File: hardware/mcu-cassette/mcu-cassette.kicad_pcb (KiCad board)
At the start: 2 copper layers, 80.4 x 50 mm, 11 parts, among them U1 02x15_PIN_HEADER_SOCKET

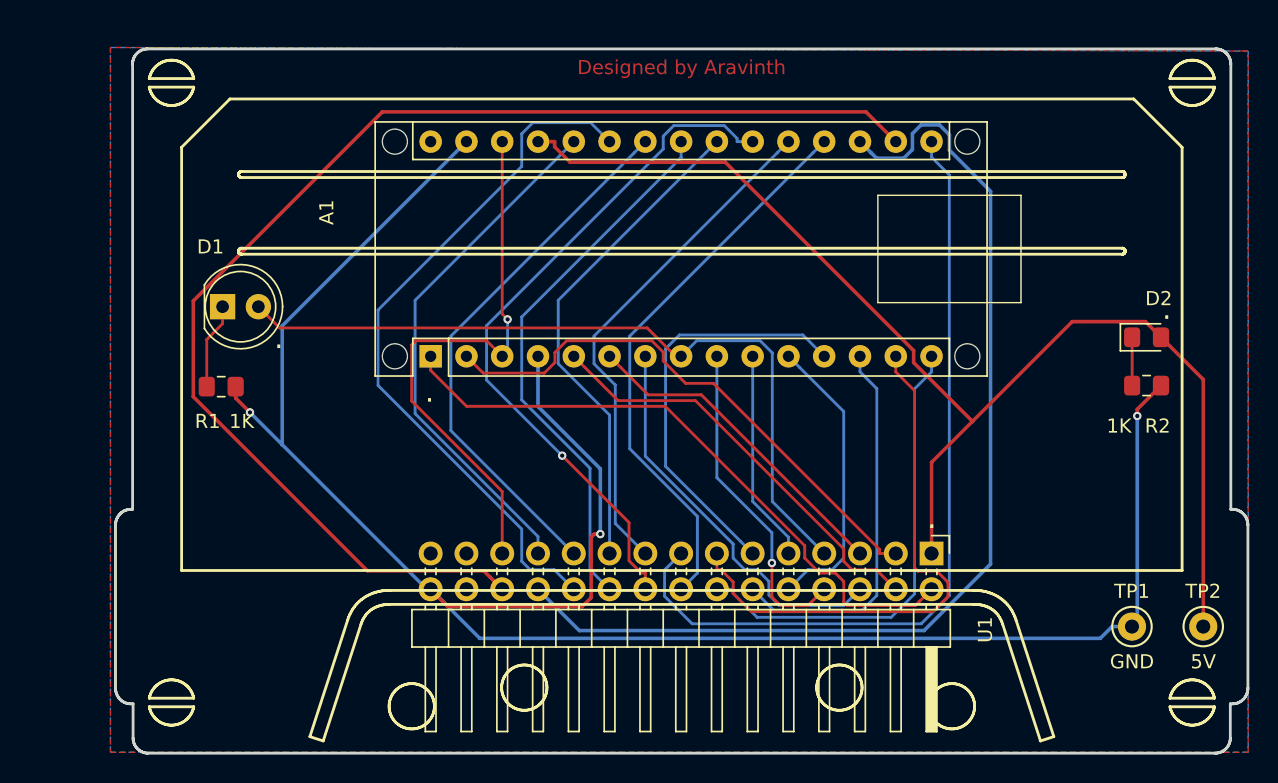
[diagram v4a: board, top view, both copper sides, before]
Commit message: [hw] Make MCU Module production ready
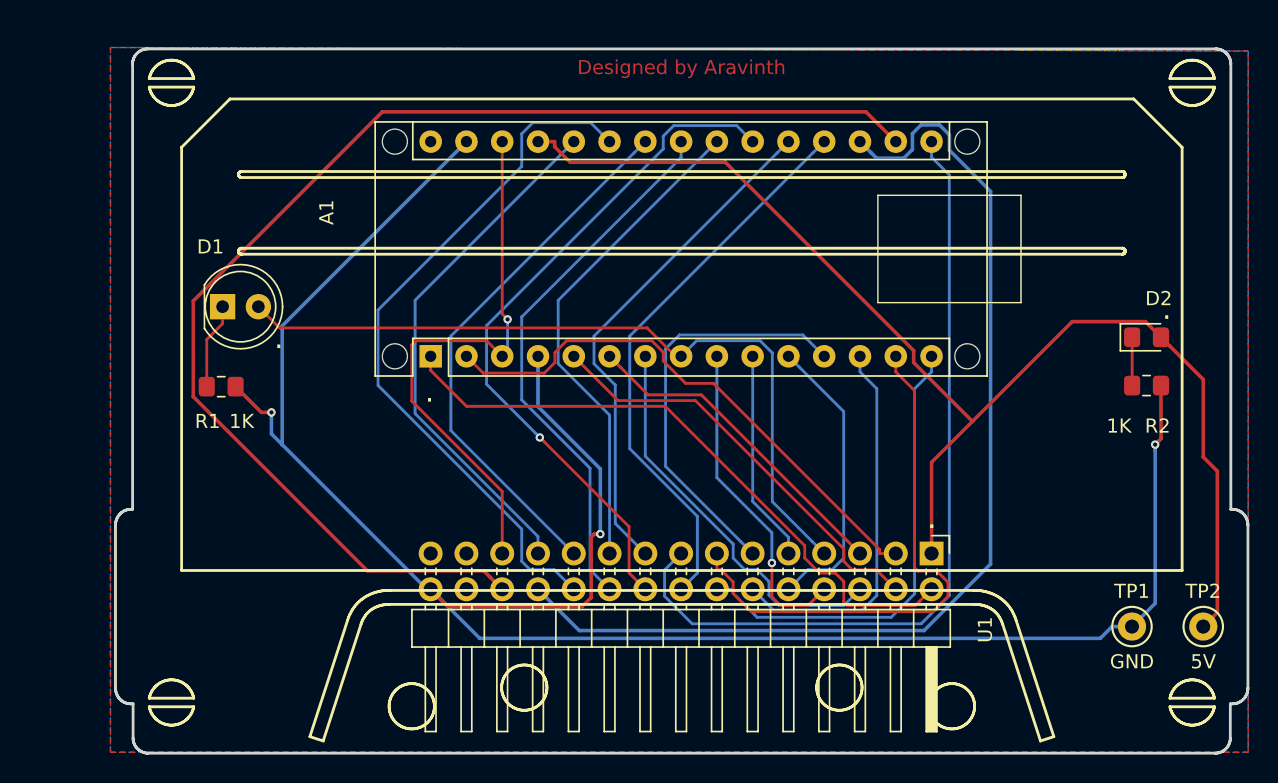
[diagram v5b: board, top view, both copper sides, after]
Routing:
- net 5V: track 88.9 -> 89.8 mm
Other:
- board text added: "MCU Module v0.1 : Designed by Aravinth"
- board text removed: "ECG Module v0.2 : Designed by Aravinth"
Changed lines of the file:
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@@
     (thickness 1.6)
     (drawings 7)
-    (tracks 256)
+    (tracks 263)
     (zones 0)
     (modules 11)
@@
     (visible_elements FFFFFF7F)
     (pcbplotparams
-      (layerselection 0x010fc_ffffffff)
-      (usegerberextensions false)
+      (layerselection 0x010f0_ffffffff)
+      (usegerberextensions true)
       (usegerberattributes false)
       (usegerberadvancedattributes false)
       (creategerberjobfile false)
-      (excludeedgelayer true)
+      (excludeedgelayer false)
       (linewidth 0.100000)
       (plotframeref false)
@@
       (plotinvisibletext false)
       (padsonsilk false)
-      (subtractmaskfromsilk false)
+      (subtractmaskfromsilk true)
       (outputformat 1)
       (mirror false)
-      (drillshape 1)
+      (drillshape 0)
       (scaleselection 1)
-      (outputdirectory ""))
+      (outputdirectory "gerber/"))
   )
   (net 0 "")
@@
     (effects (font (size 1.5 1.5) (thickness 0.3)) (justify mirror))
   )
-  (gr_text "ECG Module v0.2 : Designed by Aravinth" (at 140.4112 111.90732) (layer B.SilkS)
+  (gr_text "MCU Module v0.1 : Designed by Aravinth" (at 140.4112 111.90732) (layer B.SilkS)
     (effects (font (size 1.5 1.5) (thickness 0.3)) (justify mirror))
   )
@@
   (segment (start 140.335 138.54) (end 141.489801 137.385199) (width 0.2032) (layer B.Cu) (net 5) (status 10))
   (segment (start 172.344 141.188) (end 171.4965 141.188) (width 0.254) (layer F.Cu) (net 6) (status 30))
-  (segment (start 108.708 124.964) (end 109.728 125.984) (width 0.254) (layer F.Cu) (net 6))
-  (via (at 109.728 125.984) (size 0.6) (drill 0.3) (layers F.Cu B.Cu) (net 6))
-  (segment (start 108.708 124.155) (end 108.708 124.964) (width 0.254) (layer F.Cu) (net 6) (status 10))
   (segment (start 122.284 138.54) (end 122.555 138.54) (width 0.254) (layer B.Cu) (net 6) (status 30))
   (segment (start 112.014 119.841) (end 112.014 128.27) (width 0.254) (layer B.Cu) (net 6))
   (segment (start 112.014 128.27) (end 122.284 138.54) (width 0.254) (layer B.Cu) (net 6) (status 20))
   (segment (start 125.095 106.76) (end 112.014 119.841) (width 0.254) (layer B.Cu) (net 6) (status 10))
-  (segment (start 109.728 125.984) (end 112.014 128.27) (width 0.254) (layer B.Cu) (net 6))
   (segment (start 170.929787 141.188) (end 172.344 141.188) (width 0.254) (layer B.Cu) (net 6) (status 20))
   (segment (start 126.03801 142.02301) (end 170.094777 142.02301) (width 0.254) (layer B.Cu) (net 6))
   (segment (start 170.094777 142.02301) (end 170.929787 141.188) (width 0.254) (layer B.Cu) (net 6))
   (segment (start 122.555 138.54) (end 126.03801 142.02301) (width 0.254) (layer B.Cu) (net 6) (status 10))
-  (via (at 172.72 126.238) (size 0.6) (drill 0.3) (layers F.Cu B.Cu) (net 6))
-  (segment (start 172.72 125.764) (end 172.72 126.238) (width 0.254) (layer F.Cu) (net 6))
-  (segment (start 174.405 124.079) (end 172.72 125.764) (width 0.254) (layer F.Cu) (net 6) (status 10))
-  (segment (start 172.72 140.812) (end 172.344 141.188) (width 0.254) (layer B.Cu) (net 6) (status 30))
-  (segment (start 172.72 126.238) (end 172.72 140.812) (width 0.254) (layer B.Cu) (net 6) (status 20))
   (segment (start 134.5994 129.990288) (end 134.5994 134.62) (width 0.254) (layer B.Cu) (net 6))
   (via (at 134.5994 134.62) (size 0.6) (drill 0.3) (layers F.Cu B.Cu) (net 6))
@@
   (segment (start 133.946001 136.398) (end 133.946001 136.590881) (width 0.254) (layer F.Cu) (net 6))
   (segment (start 133.946001 134.849135) (end 133.946001 136.398) (width 0.254) (layer F.Cu) (net 6))
+  (via (at 173.99 128.27) (size 0.6) (drill 0.3) (layers F.Cu B.Cu) (net 6))
+  (segment (start 174.289999 127.970001) (end 173.99 128.27) (width 0.254) (layer F.Cu) (net 6))
+  (segment (start 174.405 124.079) (end 174.405 127.855) (width 0.254) (layer F.Cu) (net 6))
+  (segment (start 172.344 141.188) (end 173.99 139.542) (width 0.254) (layer B.Cu) (net 6))
+  (segment (start 174.405 127.855) (end 174.289999 127.970001) (width 0.254) (layer F.Cu) (net 6))
+  (segment (start 173.99 139.542) (end 173.99 128.694264) (width 0.254) (layer B.Cu) (net 6))
+  (segment (start 173.99 128.694264) (end 173.99 128.27) (width 0.254) (layer B.Cu) (net 6))
+  (via (at 111.252012 125.984) (size 0.6) (drill 0.3) (layers F.Cu B.Cu) (net 6))
+  (segment (start 111.252012 127.508012) (end 111.252012 126.408264) (width 0.254) (layer B.Cu) (net 6))
+  (segment (start 111.252012 126.408264) (end 111.252012 125.984) (width 0.254) (layer B.Cu) (net 6))
+  (segment (start 110.537 125.984) (end 110.827748 125.984) (width 0.254) (layer F.Cu) (net 6))
+  (segment (start 108.708 124.155) (end 110.537 125.984) (width 0.254) (layer F.Cu) (net 6))
+  (segment (start 110.827748 125.984) (end 111.252012 125.984) (width 0.254) (layer F.Cu) (net 6))
+  (segment (start 112.014 128.27) (end 111.252012 127.508012) (width 0.254) (layer B.Cu) (net 6))
   (segment (start 147.155001 107.559999) (end 147.955 106.76) (width 0.2032) (layer B.Cu) (net 7) (status 30))
   (segment (start 134.150199 122.530305) (end 134.150199 120.564801) (width 0.2032) (layer B.Cu) (net 7))
@@
   (segment (start 151.880199 136.554305) (end 151.880199 135.676093) (width 0.2032) (layer F.Cu) (net 8))
   (segment (start 155.575 138.54) (end 154.189801 137.154801) (width 0.2032) (layer F.Cu) (net 8) (status 10))
-  (segment (start 137.795 137.3849) (end 137.5061 137.3849) (width 0.2032) (layer F.Cu) (net 9))
-  (segment (start 136.6399 136.5187) (end 136.6399 133.801) (width 0.2032) (layer F.Cu) (net 9))
-  (segment (start 137.795 138.54) (end 137.795 137.3849) (width 0.2032) (layer F.Cu) (net 9) (status 10))
-  (segment (start 137.5061 137.3849) (end 136.6399 136.5187) (width 0.2032) (layer F.Cu) (net 9))
-  (segment (start 136.6399 133.801) (end 131.8919 129.053) (width 0.2032) (layer F.Cu) (net 9))
-  (via (at 131.8919 129.053) (size 0.6) (drill 0.3) (layers F.Cu B.Cu) (net 9))
-  (segment (start 144.3099 106.76) (end 144.3099 106.531) (width 0.2032) (layer B.Cu) (net 9))
-  (segment (start 139.065 106.3716) (end 139.065 107.2798) (width 0.2032) (layer B.Cu) (net 9))
-  (segment (start 126.5255 119.8193) (end 126.5255 123.6866) (width 0.2032) (layer B.Cu) (net 9))
-  (segment (start 144.3099 106.531) (end 143.4005 105.6216) (width 0.2032) (layer B.Cu) (net 9))
-  (segment (start 139.815 105.6216) (end 139.065 106.3716) (width 0.2032) (layer B.Cu) (net 9))
-  (segment (start 143.4005 105.6216) (end 139.815 105.6216) (width 0.2032) (layer B.Cu) (net 9))
-  (segment (start 145.415 106.76) (end 144.3099 106.76) (width 0.2032) (layer B.Cu) (net 9) (status 10))
+  (via (at 130.302 127.762) (size 0.6) (drill 0.3) (layers F.Cu B.Cu) (net 9))
+  (segment (start 137.795 138.54) (end 136.6399 137.3849) (width 0.2032) (layer F.Cu) (net 9))
+  (segment (start 136.6399 134.0999) (end 130.601999 128.061999) (width 0.2032) (layer F.Cu) (net 9))
+  (segment (start 130.601999 128.061999) (end 130.302 127.762) (width 0.2032) (layer F.Cu) (net 9))
+  (segment (start 145.415 106.76) (end 144.2766 105.6216) (width 0.2032) (layer B.Cu) (net 9))
   (segment (start 139.065 107.2798) (end 126.5255 119.8193) (width 0.2032) (layer B.Cu) (net 9))
-  (segment (start 126.5255 123.6866) (end 131.8919 129.053) (width 0.2032) (layer B.Cu) (net 9))
+  (segment (start 139.815 105.6216) (end 139.065 106.3716) (width 0.2032) (layer B.Cu) (net 9))
+  (segment (start 144.2766 105.6216) (end 139.815 105.6216) (width 0.2032) (layer B.Cu) (net 9))
+  (segment (start 130.002001 127.462001) (end 130.302 127.762) (width 0.2032) (layer B.Cu) (net 9))
+  (segment (start 126.5255 123.9855) (end 130.002001 127.462001) (width 0.2032) (layer B.Cu) (net 9))
+  (segment (start 139.065 106.3716) (end 139.065 107.2798) (width 0.2032) (layer B.Cu) (net 9))
+  (segment (start 136.6399 137.3849) (end 136.6399 134.0999) (width 0.2032) (layer F.Cu) (net 9))
+  (segment (start 126.5255 119.8193) (end 126.5255 123.9855) (width 0.2032) (layer B.Cu) (net 9))
   (segment (start 136.054999 122.799999) (end 135.255 122) (width 0.2032) (layer F.Cu) (net 10) (status 30))
   (segment (start 137.9925 124.7375) (end 136.054999 122.799999) (width 0.2032) (layer F.Cu) (net 10) (status 20))
@@
   (segment (start 131.3563 107.1271) (end 131.3563 106.76) (width 0.254) (layer F.Cu) (net 21))
   (segment (start 130.175 106.76) (end 131.3563 106.76) (width 0.254) (layer F.Cu) (net 21) (status 10))
-  (segment (start 177.404 141.188) (end 177.404 123.649) (width 0.254) (layer F.Cu) (net 21) (status 10))
-  (segment (start 177.404 123.649) (end 174.405 120.65) (width 0.254) (layer F.Cu) (net 21) (status 20))
+  (segment (start 175.028372 121.273372) (end 174.405 120.65) (width 0.254) (layer F.Cu) (net 21))
+  (segment (start 178.403999 140.188001) (end 178.403999 130.152117) (width 0.254) (layer F.Cu) (net 21))
+  (segment (start 177.404 141.188) (end 178.403999 140.188001) (width 0.254) (layer F.Cu) (net 21))
+  (segment (start 177.404 129.152118) (end 177.404 123.649) (width 0.254) (layer F.Cu) (net 21))
+  (segment (start 178.403999 130.152117) (end 177.404 129.152118) (width 0.254) (layer F.Cu) (net 21))
+  (segment (start 177.404 123.649) (end 175.028372 121.273372) (width 0.254) (layer F.Cu) (net 21))
   (segment (start 144.565001 135.150001) (end 145.415 136) (width 0.2032) (layer B.Cu) (net 22) (status 30))
   (segment (start 139.230199 129.815199) (end 144.565001 135.150001) (width 0.2032) (layer B.Cu) (net 22) (status 20))

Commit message: [hw] Make MCU Module production ready
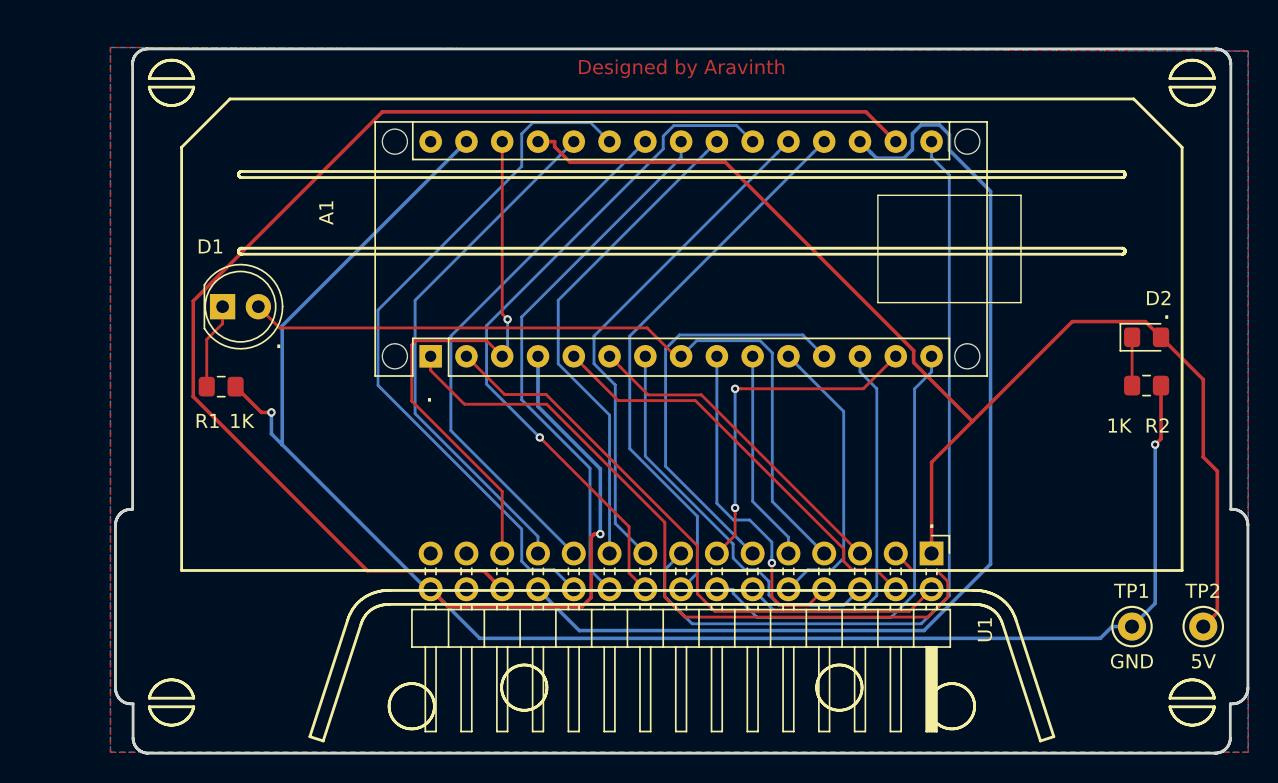
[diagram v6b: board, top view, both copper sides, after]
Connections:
- U1 pad 2: D1 -> D0
- U1 pad 3: D0 -> D1
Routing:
- net D11: track 39.1 -> 24.6 mm, vias 0 -> 2
- net D1: track 45.3 -> 54.3 mm
- net D0: track 39.1 -> 43.4 mm
- net D6: track 23.2 -> 23.8 mm
